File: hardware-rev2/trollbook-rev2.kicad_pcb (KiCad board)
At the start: 4 copper layers, 100 x 100 mm, 143 parts, among them CON1 FPGA JTAG, CON2 CPU JTAG, P1 /BR, P2 /CDIS, P3 Audio, P4 ER-CON40HT-1, P5 Power, P6 Peripheral, P7 VGA, P8 Clocks, P9 CONN_01X05, Q1 2N7002E, Q2 2N7002E, Q3 DMP3030SN-7, Q4 2N7002E, Q5 2N7002E, U1 MC68040FC33V, U10 ADA4851-4, U11 33 MHz, U12 12.288 MHz, U2 EPF10K50VRC240, U3 EPC2, U4 HY57V561620, U5 HY57V561620, U6 AS7C34098, U7 74LVC138, U8 MCP4902, U9 S25FL204K0TMFI010

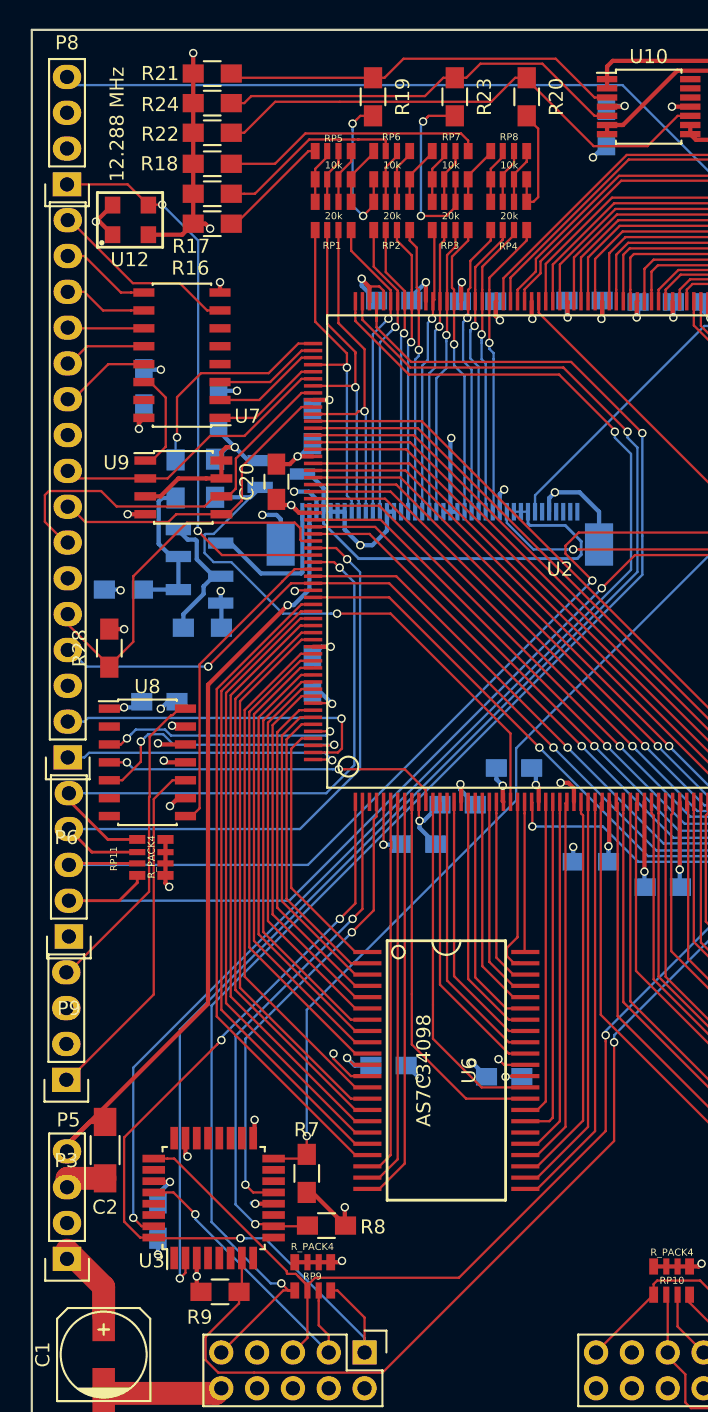
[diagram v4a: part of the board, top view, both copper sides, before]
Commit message: aligned pin headers
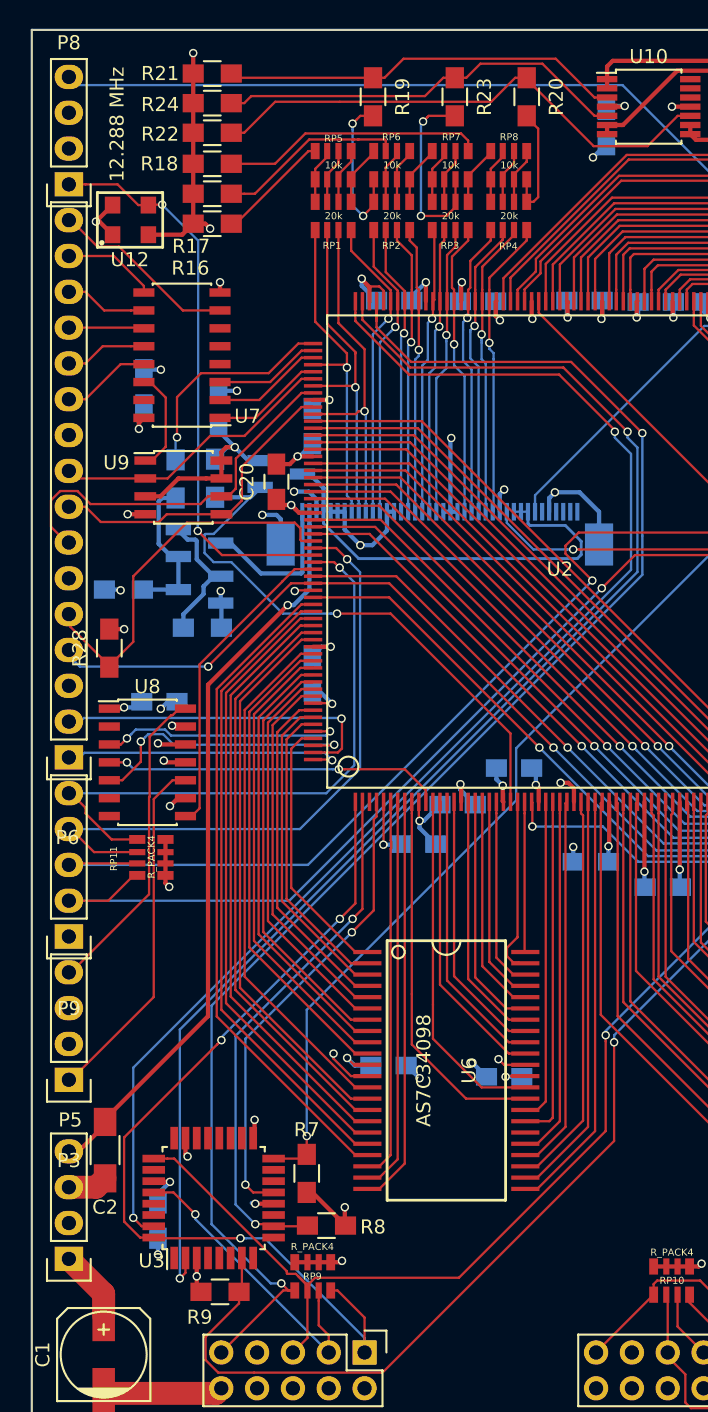
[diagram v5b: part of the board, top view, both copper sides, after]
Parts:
- moved P3 0.18 mm to (87.6, 124.5)
- moved P5 0.13 mm to (87.6, 137.2)
- moved P8 0.13 mm to (87.6, 61.0)
- moved P6 0.08 mm to (87.6, 101.6)
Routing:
- net /VGALED_ANODE: track 55.4 -> 53.1 mm
- net GND: track 406.1 -> 404.7 mm
- net +3V3: track 379.7 -> 379.0 mm
- net /SPI0CLK: track 28.5 -> 27.8 mm
- net /SPI0SS2: track 7.41 -> 6.80 mm

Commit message: finished all routing, only minor touch-ups left
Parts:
- added R34: 10k, Resistors_SMD:R_0805_HandSoldering, B.Cu at (137.7, 94.0)
- added R35: 10k, Resistors_SMD:R_0805_HandSoldering, B.Cu at (108.1, 95.5)
- added R36: 10k, Resistors_SMD:R_0805_HandSoldering, B.Cu at (136.9, 79.2)
- added REF**: 1pin, Connect:1pin, F.Cu at (115.0, 146.0)
- added REF**: 1pin, Connect:1pin, F.Cu at (181.0, 70.0)
- added REF**: 1pin, Connect:1pin, F.Cu at (181.0, 146.0)
- added REF**: MountingHole_2-5mm, Mounting_Holes:MountingHole_2-5mm, F.Cu at (102.0, 67.0)
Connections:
- U10 pad 12: (no net) -> GND
- U10 pad 13: (no net) -> +3V3
- U10 pad 4: +3V3 -> /VGADISP
- U2 pad 59: (no net) -> Net-(R34-Pad2)
- U7 pad 4: (no net) -> GND
- U7 pad 5: (no net) -> GND
- U7 pad 6: (no net) -> +3V3
- U8 pad 9: +3V3 -> /RAMCKE
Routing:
- net /RAMCKE: track 34.2 -> 99.3 mm, vias 2 -> 6
- net /VGADISP: track 30.9 -> 63.0 mm, vias 0 -> 1
- net +3V3: track 379.0 -> 390.0 mm, vias 88 -> 89
- net Net-(R34-Pad2): track 0.00 -> 10.4 mm, vias 0 -> 1
- net GND: track 404.7 -> 413.5 mm
- net /LLCE: track 27.9 -> 30.9 mm, vias 0 -> 1
- net /EXTINT1: track 71.9 -> 74.2 mm
- net /EXTINT2: track 46.0 -> 46.6 mm
- net Net-(R23-Pad1): track 29.3 -> 29.9 mm

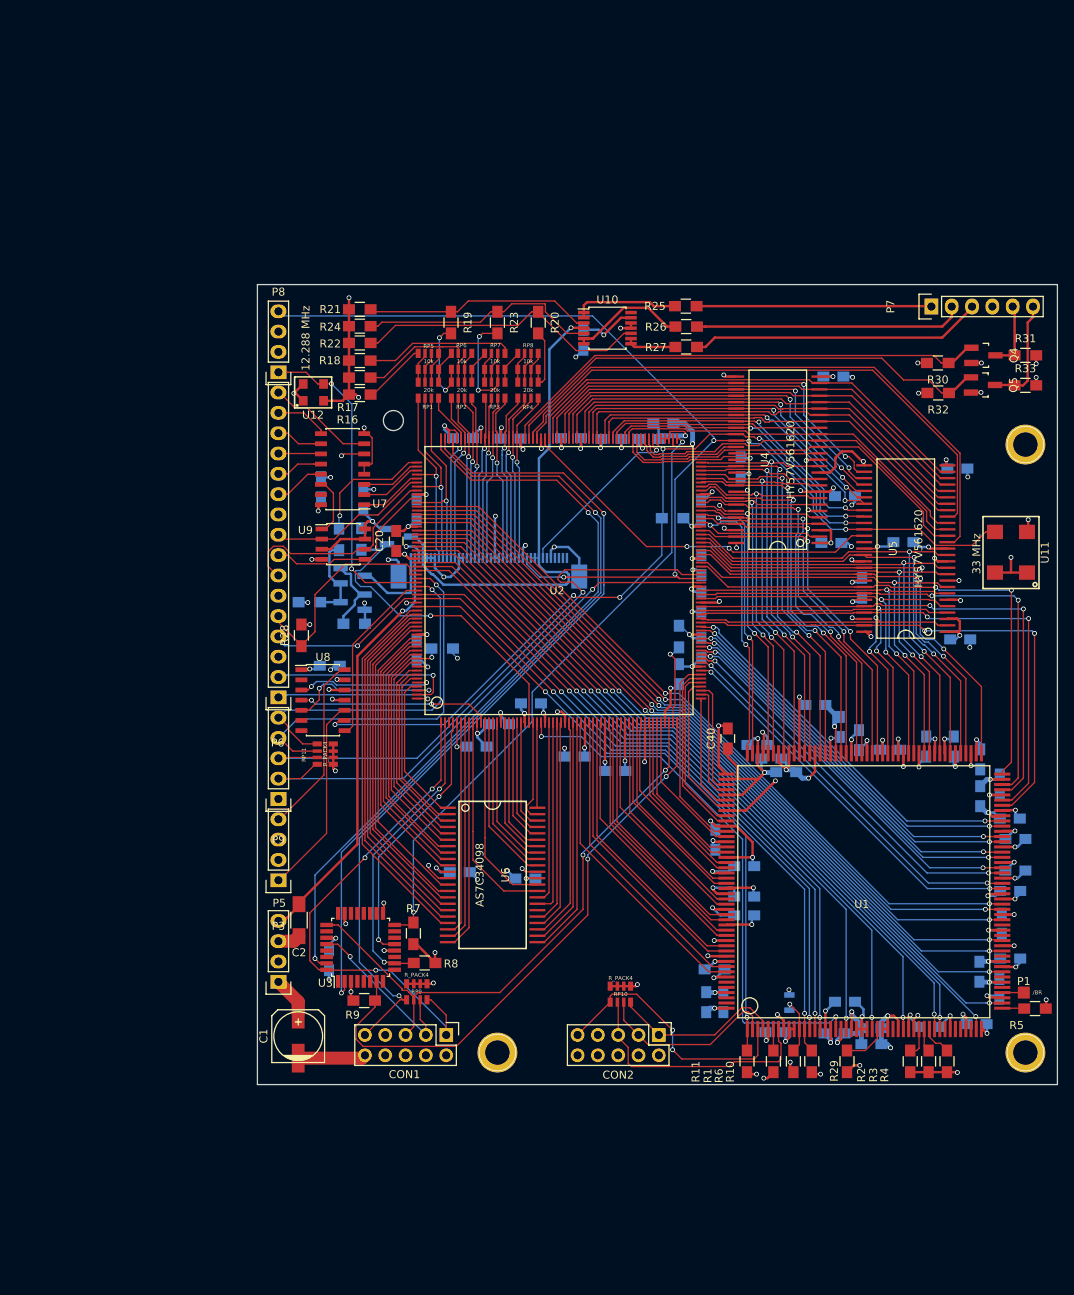
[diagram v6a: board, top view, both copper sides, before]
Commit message: touched up silkscreen a bit
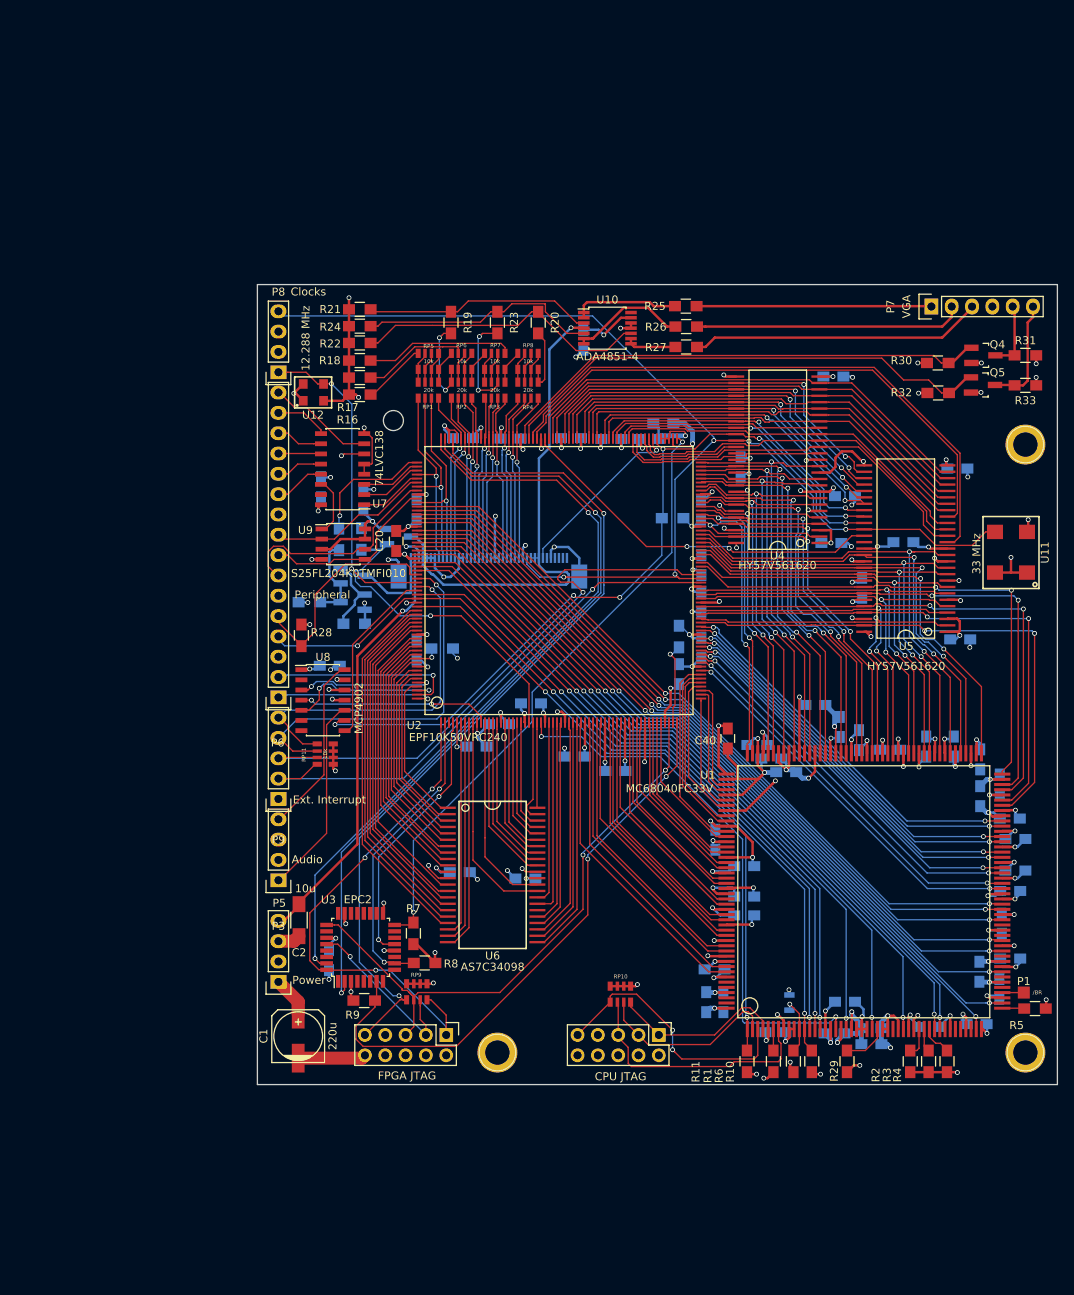
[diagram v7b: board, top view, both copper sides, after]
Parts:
- P9: value CONN_01X05 -> Ext. Interrupt
- RP10, RP11, RP9: value R_PACK4 -> 10k
